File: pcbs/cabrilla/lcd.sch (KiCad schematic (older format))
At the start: 9 parts, among them J10 Conn_01x06, J11 Conn_01x08, J12 Conn_01x10, J6 UART_LCD, J9 Conn_01x08, U2 LCD, Y1 lcd

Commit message: Added STM32
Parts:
- added R15: 10k, Resistor_SMD:R_0805_2012Metric_Pad1.15x1.40mm_HandSolder, symbol Device:R
- added SW2: SW_Push, Button_Switch_SMD:SW_Push_1P1T_NO_6x6mm_H9.5mm, symbol Switch:SW_Push
- C4: renamed from C2; footprint Capacitor_SMD:C_0805_2012Metric -> Capacitor_SMD:C_0805_2012Metric_Pad1.15x1.40mm_HandSolder
- C5: renamed from C3; footprint Capacitor_SMD:C_0805_2012Metric -> Capacitor_SMD:C_0805_2012Metric_Pad1.15x1.40mm_HandSolder
- renumbered J12 to J10, J9 to J7, J10 to J8, J11 to J9, U2 to LCD1, J6 to deb_lcd1
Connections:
- net +3V3: now also R15.1
- net GND: now also SW2.2
- net rx_lcd: now also LCD1.3 (PD1); no longer LCD1.2 (PD0)
- net tx_lcd: now also LCD1.2 (PD0); no longer LCD1.3 (PD1)
- net at LCD1.1 (PC6/~RESET): now also R15.2, SW2.1
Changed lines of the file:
@@
 P 6350 5200
 AR Path="/5D8D4EE8" Ref="#PWR?"  Part="1"
-AR Path="/5D8CC6A3/5D8D4EE8" Ref="#PWR0105"  Part="1"
-F 0 "#PWR0105" H 6350 4950 50  0001 C CNN
+AR Path="/5D8CC6A3/5D8D4EE8" Ref="#PWR019"  Part="1"
+F 0 "#PWR019" H 6350 4950 50  0001 C CNN
 F 1 "GND" H 6355 5027 50  0000 C CNN
 F 2 "" H 6350 5200 50  0001 C CNN
@@
 	6300 5200 6400 5200
 Text Label 7150 4050 2    50   ~ 0
+tx_lcd
+Text Label 7150 4150 2    50   ~ 0
 rx_lcd
-Text Label 7150 4150 2    50   ~ 0
-tx_lcd
 Wire Wire Line
 	6900 4050 7150 4050
@@
 AR Path="/5D989311/5D8D4EF4" Ref="#PWR?"  Part="1"
 AR Path="/5D8D4EF4" Ref="#PWR?"  Part="1"
-AR Path="/5D8CC6A3/5D8D4EF4" Ref="#PWR0106"  Part="1"
-F 0 "#PWR0106" H 1450 7000 50  0001 C CNN
+AR Path="/5D8CC6A3/5D8D4EF4" Ref="#PWR021"  Part="1"
+F 0 "#PWR021" H 1450 7000 50  0001 C CNN
 F 1 "GND" H 1455 7077 50  0000 C CNN
 F 2 "" H 1450 7250 50  0001 C CNN
@@
 AR Path="/5D989311/5D8D4F02" Ref="C?"  Part="1"
 AR Path="/5D8D4F02" Ref="C?"  Part="1"
-AR Path="/5D8CC6A3/5D8D4F02" Ref="C2"  Part="1"
-F 0 "C2" V 1552 7000 50  0000 C CNN
+AR Path="/5D8CC6A3/5D8D4F02" Ref="C4"  Part="1"
+F 0 "C4" V 1552 7000 50  0000 C CNN
 F 1 "22pF" V 1461 7000 50  0000 C CNN
-F 2 "Capacitor_SMD:C_0805_2012Metric" H 1338 6850 50  0001 C CNN
+F 2 "Capacitor_SMD:C_0805_2012Metric_Pad1.15x1.40mm_HandSolder" H 1338 6850 50  0001 C CNN
 F 3 "~" H 1300 7000 50  0001 C CNN
 	1    1300 7000
@@
 AR Path="/5D989311/5D8D4F08" Ref="C?"  Part="1"
 AR Path="/5D8D4F08" Ref="C?"  Part="1"
-AR Path="/5D8CC6A3/5D8D4F08" Ref="C3"  Part="1"
-F 0 "C3" V 1440 7000 50  0000 C CNN
+AR Path="/5D8CC6A3/5D8D4F08" Ref="C5"  Part="1"
+F 0 "C5" V 1440 7000 50  0000 C CNN
 F 1 "22pF" V 1349 7000 50  0000 C CNN
-F 2 "Capacitor_SMD:C_0805_2012Metric" H 1638 6850 50  0001 C CNN
+F 2 "Capacitor_SMD:C_0805_2012Metric_Pad1.15x1.40mm_HandSolder" H 1638 6850 50  0001 C CNN
 F 3 "~" H 1600 7000 50  0001 C CNN
 	1    1600 7000
@@
 $EndComp
 $Comp
-L MCU_Microchip_ATmega:ATmega8A-PU U?
+L MCU_Microchip_ATmega:ATmega8A-PU LCD?
 U 1 1 5D8D4F18
 P 6300 3750
-AR Path="/5D8D4F18" Ref="U?"  Part="1"
-AR Path="/5D8CC6A3/5D8D4F18" Ref="U2"  Part="1"
-F 0 "U2" H 6300 5331 50  0000 C CNN
+AR Path="/5D8D4F18" Ref="LCD?"  Part="1"
+AR Path="/5D8CC6A3/5D8D4F18" Ref="LCD1"  Part="1"
+F 0 "LCD1" H 6300 5331 50  0000 C CNN
 F 1 "LCD" H 6300 5240 50  0000 C CNN
 F 2 "Package_DIP:DIP-28_W7.62mm_Socket" H 6300 3750 50  0001 C CIN
@@
 rx_lcd
 $Comp
-L Connector:Conn_01x03_Male J?
+L Connector:Conn_01x03_Male deb_lcd?
 U 1 1 5D8D615F
 P 2800 6450
-AR Path="/5D8D615F" Ref="J?"  Part="1"
-AR Path="/5D8CC6A3/5D8D615F" Ref="J6"  Part="1"
-F 0 "J6" V 2862 6594 50  0000 L CNN
+AR Path="/5D8D615F" Ref="deb_lcd?"  Part="1"
+AR Path="/5D8CC6A3/5D8D615F" Ref="deb_lcd1"  Part="1"
+F 0 "deb_lcd1" V 2862 6594 50  0000 L CNN
 F 1 "UART_LCD" V 2953 6594 50  0000 L CNN
 F 2 "Connector_PinHeader_2.54mm:PinHeader_1x03_P2.54mm_Vertical" H 2800 6450 50  0001 C CNN
@@
 P 2900 6750
 AR Path="/5D8D6166" Ref="#PWR?"  Part="1"
-AR Path="/5D8CC6A3/5D8D6166" Ref="#PWR0107"  Part="1"
-F 0 "#PWR0107" H 2900 6500 50  0001 C CNN
+AR Path="/5D8CC6A3/5D8D6166" Ref="#PWR020"  Part="1"
+F 0 "#PWR020" H 2900 6500 50  0001 C CNN
 F 1 "GND" H 2905 6577 50  0000 C CNN
 F 2 "" H 2900 6750 50  0001 C CNN
@@
 $EndComp
 Text HLabel 7150 4150 2    50   Input ~ 0
+rx_lcd
+Text HLabel 7150 4050 2    50   Input ~ 0
 tx_lcd
-Text HLabel 7150 4050 2    50   Input ~ 0
-rx_lcd
-$Comp
-L power:+3.3V #PWR0103
+$Comp
+L power:+3.3V #PWR018
 U 1 1 5D8AEFC8
 P 6350 2100
-F 0 "#PWR0103" H 6350 1950 50  0001 C CNN
+F 0 "#PWR018" H 6350 1950 50  0001 C CNN
 F 1 "+3.3V" H 6365 2273 50  0000 C CNN
 F 2 "" H 6350 2100 50  0001 C CNN
@@
 osc_2
 $Comp
-L Connector_Generic:Conn_01x08 J9
+L Connector_Generic:Conn_01x08 J7
 U 1 1 5D8BEC29
 P 800 1150
-F 0 "J9" H 718 525 50  0000 C CNN
+F 0 "J7" H 718 525 50  0000 C CNN
 F 1 "Conn_01x08" H 718 616 50  0000 C CNN
 F 2 "Connector_Molex:Molex_KK-254_AE-6410-08A_1x08_P2.54mm_Vertical" H 800 1150 50  0001 C CNN
@@
 $EndComp
 $Comp
-L Connector_Generic:Conn_01x06 J10
+L Connector_Generic:Conn_01x06 J8
 U 1 1 5D8C0CBE
 P 800 2100
-F 0 "J10" H 718 1575 50  0000 C CNN
+F 0 "J8" H 718 1575 50  0000 C CNN
 F 1 "Conn_01x06" H 718 1666 50  0000 C CNN
 F 2 "Connector_Molex:Molex_KK-254_AE-6410-06A_1x06_P2.54mm_Vertical" H 800 2100 50  0001 C CNN
@@
 $EndComp
 $Comp
-L Connector_Generic:Conn_01x08 J11
+L Connector_Generic:Conn_01x08 J9
 U 1 1 5D8C1CF3
 P 800 3100
-F 0 "J11" H 718 2475 50  0000 C CNN
+F 0 "J9" H 718 2475 50  0000 C CNN
 F 1 "Conn_01x08" H 718 2566 50  0000 C CNN
 F 2 "Connector_Molex:Molex_KK-254_AE-6410-08A_1x08_P2.54mm_Vertical" H 800 3100 50  0001 C CNN
@@
 $EndComp
 $Comp
-L Connector_Generic:Conn_01x10 J12
+L Connector_Generic:Conn_01x10 J10
 U 1 1 5D8C21ED
 P 800 4250
-F 0 "J12" H 718 3525 50  0000 C CNN
+F 0 "J10" H 718 3525 50  0000 C CNN
 F 1 "Conn_01x10" H 718 3616 50  0000 C CNN
 F 2 "Connector_Molex:Molex_KK-254_AE-6410-10A_1x10_P2.54mm_Vertical" H 800 4250 50  0001 C CNN
@@
 	-1   0    0    1
 $EndComp
+$Comp
+L Switch:SW_Push SW?
+U 1 1 5D92708E
+P 4350 2850
+AR Path="/5D8ABBE4/5D92708E" Ref="SW?"  Part="1"
+AR Path="/5D8CC6A3/5D92708E" Ref="SW2"  Part="1"
+F 0 "SW2" V 4304 2998 50  0000 L CNN
+F 1 "SW_Push" V 4395 2998 50  0000 L CNN
+F 2 "Button_Switch_SMD:SW_Push_1P1T_NO_6x6mm_H9.5mm" H 4350 3050 50  0001 C CNN
+F 3 "~" H 4350 3050 50  0001 C CNN
+	1    4350 2850
+	0    1    1    0
+$EndComp
+$Comp
+L Device:R R?
+U 1 1 5D927094
+P 4350 2500
+AR Path="/5D8ABBE4/5D927094" Ref="R?"  Part="1"
+AR Path="/5D8CC6A3/5D927094" Ref="R15"  Part="1"
+F 0 "R15" H 4420 2546 50  0000 L CNN
+F 1 "10k" H 4420 2455 50  0000 L CNN
+F 2 "Resistor_SMD:R_0805_2012Metric_Pad1.15x1.40mm_HandSolder" V 4280 2500 50  0001 C CNN
+F 3 "~" H 4350 2500 50  0001 C CNN
+	1    4350 2500
+	1    0    0    -1
+$EndComp
+Connection ~ 4350 2650
+Wire Wire Line
+	4350 2650 5700 2650
+$Comp
+L power:GND #PWR?
+U 1 1 5D92709C
+P 4350 3050
+AR Path="/5D8ABBE4/5D92709C" Ref="#PWR?"  Part="1"
+AR Path="/5D8CC6A3/5D92709C" Ref="#PWR029"  Part="1"
+F 0 "#PWR029" H 4350 2800 50  0001 C CNN
+F 1 "GND" H 4355 2877 50  0000 C CNN
+F 2 "" H 4350 3050 50  0001 C CNN
+F 3 "" H 4350 3050 50  0001 C CNN
+	1    4350 3050
+	1    0    0    -1
+$EndComp
+$Comp
+L power:+3.3V #PWR?
+U 1 1 5D9270A2
+P 4350 2350
+AR Path="/5D8ABBE4/5D9270A2" Ref="#PWR?"  Part="1"
+AR Path="/5D8CC6A3/5D9270A2" Ref="#PWR028"  Part="1"
+F 0 "#PWR028" H 4350 2200 50  0001 C CNN
+F 1 "+3.3V" H 4365 2523 50  0000 C CNN
+F 2 "" H 4350 2350 50  0001 C CNN
+F 3 "" H 4350 2350 50  0001 C CNN
+	1    4350 2350
+	1    0    0    -1
+$EndComp
 $EndSCHEMATC

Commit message: ixed
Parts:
- Y1: footprint Crystal:Crystal_HC49-4H_Vertical -> Crystal:Crystal_SMD_HC49-SD_HandSoldering
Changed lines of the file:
@@
 F 0 "Y1" H 1450 6918 50  0000 C CNN
 F 1 "lcd" H 1450 6827 50  0000 C CNN
-F 2 "Crystal:Crystal_HC49-4H_Vertical" H 1450 6650 50  0001 C CNN
+F 2 "Crystal:Crystal_SMD_HC49-SD_HandSoldering" H 1450 6650 50  0001 C CNN
 F 3 "~" H 1450 6650 50  0001 C CNN
 	1    1450 6650

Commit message: 80
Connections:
- net rx_lcd: now also LCD1.2 (PD0); no longer LCD1.3 (PD1)
- net tx_lcd: now also LCD1.3 (PD1); no longer LCD1.2 (PD0)
- net RD: now reaches J8.1 (Pin_1)
- net RD: now also LCD1.23 (PC0)
- net WR: now reaches J8.2 (Pin_2)
- net WR: now also LCD1.24 (PC1)
- net RS: now reaches J8.3 (Pin_3)
- net RS: now also LCD1.25 (PC2)
- net CS: now reaches J8.4 (Pin_4)
- net CS: now also LCD1.26 (PC3)
- net RST: now reaches J8.5 (Pin_5)
- net RST: now also LCD1.27 (PC4)
- no-connect marks 0 -> 2
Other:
- moved on the sheet: R15, SW2
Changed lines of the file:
@@
 	6300 5200 6400 5200
 Text Label 7150 4050 2    50   ~ 0
+rx_lcd
+Text Label 7150 4150 2    50   ~ 0
 tx_lcd
-Text Label 7150 4150 2    50   ~ 0
-rx_lcd
 Wire Wire Line
 	6900 4050 7150 4050
@@
 $EndComp
 Text HLabel 7150 4150 2    50   Input ~ 0
+tx_lcd
+Text HLabel 7150 4050 2    50   Input ~ 0
 rx_lcd
-Text HLabel 7150 4050 2    50   Input ~ 0
-tx_lcd
 $Comp
 L power:+3.3V #PWR018
@@
 L Switch:SW_Push SW?
 U 1 1 5D92708E
-P 4350 2850
+P 5100 2850
 AR Path="/5D8ABBE4/5D92708E" Ref="SW?"  Part="1"
 AR Path="/5D8CC6A3/5D92708E" Ref="SW2"  Part="1"
-F 0 "SW2" V 4304 2998 50  0000 L CNN
-F 1 "SW_Push" V 4395 2998 50  0000 L CNN
-F 2 "Button_Switch_SMD:SW_Push_1P1T_NO_6x6mm_H9.5mm" H 4350 3050 50  0001 C CNN
-F 3 "~" H 4350 3050 50  0001 C CNN
-	1    4350 2850
+F 0 "SW2" V 5054 2998 50  0000 L CNN
+F 1 "SW_Push" V 5145 2998 50  0000 L CNN
+F 2 "Button_Switch_SMD:SW_Push_1P1T_NO_6x6mm_H9.5mm" H 5100 3050 50  0001 C CNN
+F 3 "~" H 5100 3050 50  0001 C CNN
+	1    5100 2850
 	0    1    1    0
 $EndComp
@@
 L Device:R R?
 U 1 1 5D927094
-P 4350 2500
+P 5100 2500
 AR Path="/5D8ABBE4/5D927094" Ref="R?"  Part="1"
 AR Path="/5D8CC6A3/5D927094" Ref="R15"  Part="1"
-F 0 "R15" H 4420 2546 50  0000 L CNN
-F 1 "10k" H 4420 2455 50  0000 L CNN
-F 2 "Resistor_SMD:R_0805_2012Metric_Pad1.15x1.40mm_HandSolder" V 4280 2500 50  0001 C CNN
-F 3 "~" H 4350 2500 50  0001 C CNN
-	1    4350 2500
-	1    0    0    -1
-$EndComp
-Connection ~ 4350 2650
-Wire Wire Line
-	4350 2650 5700 2650
+F 0 "R15" H 5170 2546 50  0000 L CNN
+F 1 "10k" H 5170 2455 50  0000 L CNN
+F 2 "Resistor_SMD:R_0805_2012Metric_Pad1.15x1.40mm_HandSolder" V 5030 2500 50  0001 C CNN
+F 3 "~" H 5100 2500 50  0001 C CNN
+	1    5100 2500
+	1    0    0    -1
+$EndComp
+Connection ~ 5100 2650
+Wire Wire Line
+	5100 2650 5700 2650
 $Comp
 L power:GND #PWR?
 U 1 1 5D92709C
-P 4350 3050
+P 5100 3050
 AR Path="/5D8ABBE4/5D92709C" Ref="#PWR?"  Part="1"
 AR Path="/5D8CC6A3/5D92709C" Ref="#PWR029"  Part="1"
-F 0 "#PWR029" H 4350 2800 50  0001 C CNN
-F 1 "GND" H 4355 2877 50  0000 C CNN
-F 2 "" H 4350 3050 50  0001 C CNN
-F 3 "" H 4350 3050 50  0001 C CNN
-	1    4350 3050
+F 0 "#PWR029" H 5100 2800 50  0001 C CNN
+F 1 "GND" H 5105 2877 50  0000 C CNN
+F 2 "" H 5100 3050 50  0001 C CNN
+F 3 "" H 5100 3050 50  0001 C CNN
+	1    5100 3050
 	1    0    0    -1
 $EndComp
@@
 L power:+3.3V #PWR?
 U 1 1 5D9270A2
-P 4350 2350
+P 5100 2350
 AR Path="/5D8ABBE4/5D9270A2" Ref="#PWR?"  Part="1"
 AR Path="/5D8CC6A3/5D9270A2" Ref="#PWR028"  Part="1"
-F 0 "#PWR028" H 4350 2200 50  0001 C CNN
-F 1 "+3.3V" H 4365 2523 50  0000 C CNN
-F 2 "" H 4350 2350 50  0001 C CNN
-F 3 "" H 4350 2350 50  0001 C CNN
-	1    4350 2350
-	1    0    0    -1
-$EndComp
+F 0 "#PWR028" H 5100 2200 50  0001 C CNN
+F 1 "+3.3V" H 5115 2523 50  0000 C CNN
+F 2 "" H 5100 2350 50  0001 C CNN
+F 3 "" H 5100 2350 50  0001 C CNN
+	1    5100 2350
+	1    0    0    -1
+$EndComp
+Text Label 1150 2300 0    50   ~ 0
+RD
+Text Label 1150 2000 0    50   ~ 0
+CS
+Text Label 1150 2200 0    50   ~ 0
+WR
+Text Label 1150 2100 0    50   ~ 0
+RS
+Text Label 1150 1900 0    50   ~ 0
+RST
+Wire Wire Line
+	1150 2300 1000 2300
+Wire Wire Line
+	1150 2200 1000 2200
+Wire Wire Line
+	1150 2100 1000 2100
+Wire Wire Line
+	1150 2000 1000 2000
+Wire Wire Line
+	1150 1900 1000 1900
+NoConn ~ 1000 1800
+Text Label 7050 3350 0    50   ~ 0
+RD
+Text Label 7050 3650 0    50   ~ 0
+CS
+Text Label 7050 3450 0    50   ~ 0
+WR
+Text Label 7050 3550 0    50   ~ 0
+RS
+Text Label 7050 3750 0    50   ~ 0
+RST
+Wire Wire Line
+	7050 3350 6900 3350
+Wire Wire Line
+	7050 3450 6900 3450
+Wire Wire Line
+	7050 3550 6900 3550
+Wire Wire Line
+	7050 3650 6900 3650
+Wire Wire Line
+	7050 3750 6900 3750
+NoConn ~ 6900 3850
 $EndSCHEMATC

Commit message: Updated footprints
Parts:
- Y1: footprint Crystal:Crystal_SMD_HC49-SD_HandSoldering -> Crystal:Crystal_HC49-4H_Vertical
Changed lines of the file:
@@
 EESchema Schematic File Version 4
 LIBS:cabrilla-cache
-EELAYER 30 0
+EELAYER 29 0
 EELAYER END
 $Descr A4 11693 8268
@@
 F 0 "Y1" H 1450 6918 50  0000 C CNN
 F 1 "lcd" H 1450 6827 50  0000 C CNN
-F 2 "Crystal:Crystal_SMD_HC49-SD_HandSoldering" H 1450 6650 50  0001 C CNN
+F 2 "Crystal:Crystal_HC49-4H_Vertical" H 1450 6650 50  0001 C CNN
 F 3 "~" H 1450 6650 50  0001 C CNN
 	1    1450 6650

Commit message: Routed
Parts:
- removed J10: Conn_01x10, Connector_Molex:Molex_KK-254_AE-6410-10A_1x10_P2.54mm_Vertical, symbol Connector_Generic:Conn_01x10
- added lcd_power1: lcd_power, Connector_Molex:Molex_KK-254_AE-6410-08A_1x08_P2.54mm_Vertical, symbol Connector_Generic:Conn_01x08
- J9: value Conn_01x08 -> lcd_digital1
- SW2: footprint Button_Switch_SMD:SW_Push_1P1T_NO_6x6mm_H9.5mm -> Button_Switch_SMD:SW_Push_1P1T_NO_CK_KSC6xxJ
- renumbered J8 to lcd_analog1, J7 to lcd_digital2
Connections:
- net +3V3: now also lcd_power1.4 (Pin_4)
- net CS: now also lcd_analog1.2 (Pin_2); no longer lcd_analog1.4 (Pin_4)
- net GND: now also LCD1.22 (AGND), LCD1.8 (GND), lcd_power1.6 (Pin_6), lcd_power1.7 (Pin_7)
- net RD: now also lcd_analog1.5 (Pin_5); no longer lcd_analog1.1 (Pin_1)
- net RST: now also lcd_analog1.1 (Pin_1); no longer lcd_analog1.5 (Pin_5)
- net WR: now also lcd_analog1.4 (Pin_4); no longer lcd_analog1.2 (Pin_2)
- net SCK: now reaches lcd_digital2.3 (Pin_3)
- net SCK: now also LCD1.19 (PB5)
- net DO: now reaches lcd_digital2.4 (Pin_4)
- net DO: now also LCD1.18 (PB4)
- net DI: now reaches lcd_digital2.5 (Pin_5)
- net DI: now also LCD1.17 (PB3)
- net SS: now reaches lcd_digital2.6 (Pin_6)
- net SS: now also LCD1.16 (PB2)
- net D1: now reaches lcd_digital2.7 (Pin_7)
- net D1: now also LCD1.15 (PB1)
- net D0: now reaches lcd_digital2.8 (Pin_8)
- net D0: now also LCD1.14 (PB0)
- net D2: now reaches J9.3 (Pin_3)
- net D2: now also LCD1.4 (PD2)
- net D3: now reaches J9.4 (Pin_4)
- net D3: now also LCD1.5 (PD3)
- net D4: now reaches J9.5 (Pin_5)
- net D4: now also LCD1.6 (PD4)
- net D5: now reaches J9.6 (Pin_6)
- net D5: now also LCD1.11 (PD5)
- net D6: now reaches J9.7 (Pin_7)
- net D6: now also LCD1.12 (PD6)
- net D7: now reaches J9.8 (Pin_8)
- net D7: now also LCD1.13 (PD7)
- new net +5V: lcd_power1.5 (Pin_5)
- no-connect marks 2 -> 11
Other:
- moved on the sheet: lcd_analog1, lcd_digital2

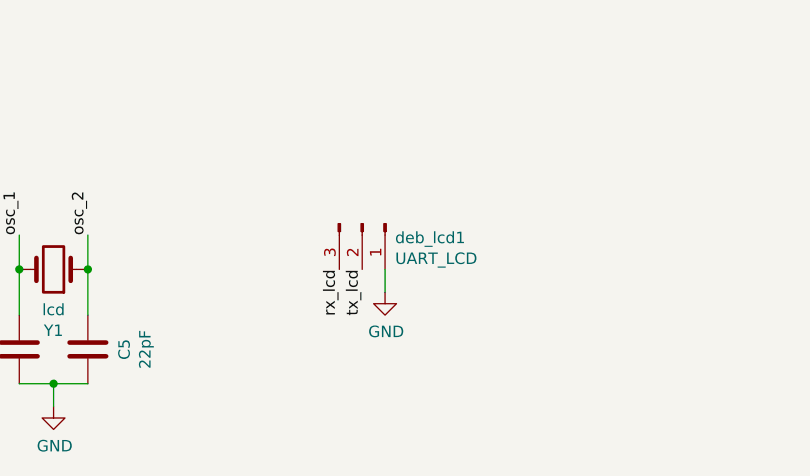
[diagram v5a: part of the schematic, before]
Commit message: Cambiados los parámetros de rutero
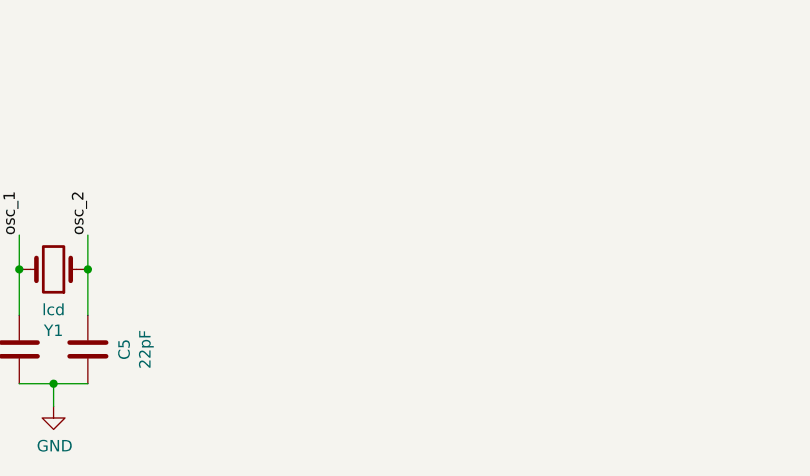
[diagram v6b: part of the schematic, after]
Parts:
- removed deb_lcd1: UART_LCD, Connector_PinHeader_2.54mm:PinHeader_1x03_P2.54mm_Vertical, symbol Connector:Conn_01x03_Male
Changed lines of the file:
@@
-	1    0    0    -1
-$EndComp
-Text Label 2800 6650 3    50   ~ 0
-tx_lcd
-Text Label 2700 6650 3    50   ~ 0
-rx_lcd
-$Comp
-L Connector:Conn_01x03_Male deb_lcd?
-U 1 1 5D8D615F
-P 2800 6450
-AR Path="/5D8D615F" Ref="deb_lcd?"  Part="1"
-AR Path="/5D8CC6A3/5D8D615F" Ref="deb_lcd1"  Part="1"
-F 0 "deb_lcd1" V 2862 6594 50  0000 L CNN
-F 1 "UART_LCD" V 2953 6594 50  0000 L CNN
-F 2 "Connector_PinHeader_2.54mm:PinHeader_1x03_P2.54mm_Vertical" H 2800 6450 50  0001 C CNN
-F 3 "~" H 2800 6450 50  0001 C CNN
-	1    2800 6450
-	0    1    1    0
-$EndComp
-Wire Wire Line
-	2900 6650 2900 6750
-$Comp
-L power:GND #PWR?
-U 1 1 5D8D6166
-P 2900 6750
-AR Path="/5D8D6166" Ref="#PWR?"  Part="1"
-AR Path="/5D8CC6A3/5D8D6166" Ref="#PWR020"  Part="1"
-F 0 "#PWR020" H 2900 6500 50  0001 C CNN
-F 1 "GND" H 2905 6577 50  0000 C CNN
-F 2 "" H 2900 6750 50  0001 C CNN
-F 3 "" H 2900 6750 50  0001 C CNN
-	1    2900 6750
 	1    0    0    -1
 $EndComp
